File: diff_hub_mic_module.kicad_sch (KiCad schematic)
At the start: 4 parts, among them J6 RJ45, U11 MAX3485_SD

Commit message: Fixed most ERC checks
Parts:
- renumbered C13 to C12, J6 to J4, U11 to U6
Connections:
- no-connect marks 0 -> 1
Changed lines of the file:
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@@
 		(color 0 0 0 0)
+	)
+	(no_connect
+		(at 92.71 63.5)
 	)
 	(wire
@@
 		(dnp no)
 		(fields_autoplaced yes)
-		(property "Reference" "#PWR050"
+		(property "Reference" "#PWR041"
 			(at 90.17 46.99 0)
 			(effects
@@
 			(project "AEC_Speaker_Mic_System"
 				(path "/b4ee80b5-9d9a-4551-9b0c-6a8cb8d78ca3/ff66f788-06df-4fa5-89ad-7a9539b69b02/4ec81307-e110-499c-8742-d662ba3b7e0b"
-					(reference "#PWR060")
+					(reference "#PWR051")
 					(unit 1)
 				)
 				(path "/b4ee80b5-9d9a-4551-9b0c-6a8cb8d78ca3/ff66f788-06df-4fa5-89ad-7a9539b69b02/9b23b194-3f15-4ab8-af8d-e9f0a2683966"
-					(reference "#PWR065")
+					(reference "#PWR056")
 					(unit 1)
 				)
 				(path "/b4ee80b5-9d9a-4551-9b0c-6a8cb8d78ca3/ff66f788-06df-4fa5-89ad-7a9539b69b02/a06cf9bb-2ae0-4081-99cc-d8b6234c3557"
-					(reference "#PWR055")
+					(reference "#PWR046")
 					(unit 1)
 				)
 				(path "/b4ee80b5-9d9a-4551-9b0c-6a8cb8d78ca3/ff66f788-06df-4fa5-89ad-7a9539b69b02/e9f22984-330c-410d-9c8a-778be080e49d"
-					(reference "#PWR050")
+					(reference "#PWR041")
 					(unit 1)
 				)
@@
 		(dnp no)
 		(fields_autoplaced yes)
-		(property "Reference" "#PWR048"
+		(property "Reference" "#PWR039"
 			(at 67.31 50.8 0)
 			(effects
@@
 			(project "AEC_Speaker_Mic_System"
 				(path "/b4ee80b5-9d9a-4551-9b0c-6a8cb8d78ca3/ff66f788-06df-4fa5-89ad-7a9539b69b02/4ec81307-e110-499c-8742-d662ba3b7e0b"
-					(reference "#PWR058")
+					(reference "#PWR049")
 					(unit 1)
 				)
 				(path "/b4ee80b5-9d9a-4551-9b0c-6a8cb8d78ca3/ff66f788-06df-4fa5-89ad-7a9539b69b02/9b23b194-3f15-4ab8-af8d-e9f0a2683966"
-					(reference "#PWR063")
+					(reference "#PWR054")
 					(unit 1)
 				)
 				(path "/b4ee80b5-9d9a-4551-9b0c-6a8cb8d78ca3/ff66f788-06df-4fa5-89ad-7a9539b69b02/a06cf9bb-2ae0-4081-99cc-d8b6234c3557"
-					(reference "#PWR053")
+					(reference "#PWR044")
 					(unit 1)
 				)
 				(path "/b4ee80b5-9d9a-4551-9b0c-6a8cb8d78ca3/ff66f788-06df-4fa5-89ad-7a9539b69b02/e9f22984-330c-410d-9c8a-778be080e49d"
-					(reference "#PWR048")
+					(reference "#PWR039")
 					(unit 1)
 				)
@@
 		(dnp no)
 		(fields_autoplaced yes)
-		(property "Reference" "#PWR049"
+		(property "Reference" "#PWR040"
 			(at 77.47 53.34 0)
 			(effects
@@
 			(project "AEC_Speaker_Mic_System"
 				(path "/b4ee80b5-9d9a-4551-9b0c-6a8cb8d78ca3/ff66f788-06df-4fa5-89ad-7a9539b69b02/4ec81307-e110-499c-8742-d662ba3b7e0b"
-					(reference "#PWR059")
+					(reference "#PWR050")
 					(unit 1)
 				)
 				(path "/b4ee80b5-9d9a-4551-9b0c-6a8cb8d78ca3/ff66f788-06df-4fa5-89ad-7a9539b69b02/9b23b194-3f15-4ab8-af8d-e9f0a2683966"
-					(reference "#PWR064")
+					(reference "#PWR055")
 					(unit 1)
 				)
 				(path "/b4ee80b5-9d9a-4551-9b0c-6a8cb8d78ca3/ff66f788-06df-4fa5-89ad-7a9539b69b02/a06cf9bb-2ae0-4081-99cc-d8b6234c3557"
-					(reference "#PWR054")
+					(reference "#PWR045")
 					(unit 1)
 				)
 				(path "/b4ee80b5-9d9a-4551-9b0c-6a8cb8d78ca3/ff66f788-06df-4fa5-89ad-7a9539b69b02/e9f22984-330c-410d-9c8a-778be080e49d"
-					(reference "#PWR049")
+					(reference "#PWR040")
 					(unit 1)
 				)
@@
 		(dnp no)
 		(fields_autoplaced yes)
-		(property "Reference" "#PWR052"
+		(property "Reference" "#PWR043"
 			(at 102.87 80.01 0)
 			(effects
@@
 			(project "AEC_Speaker_Mic_System"
 				(path "/b4ee80b5-9d9a-4551-9b0c-6a8cb8d78ca3/ff66f788-06df-4fa5-89ad-7a9539b69b02/4ec81307-e110-499c-8742-d662ba3b7e0b"
-					(reference "#PWR062")
+					(reference "#PWR053")
 					(unit 1)
 				)
 				(path "/b4ee80b5-9d9a-4551-9b0c-6a8cb8d78ca3/ff66f788-06df-4fa5-89ad-7a9539b69b02/9b23b194-3f15-4ab8-af8d-e9f0a2683966"
-					(reference "#PWR067")
+					(reference "#PWR058")
 					(unit 1)
 				)
 				(path "/b4ee80b5-9d9a-4551-9b0c-6a8cb8d78ca3/ff66f788-06df-4fa5-89ad-7a9539b69b02/a06cf9bb-2ae0-4081-99cc-d8b6234c3557"
-					(reference "#PWR057")
+					(reference "#PWR048")
 					(unit 1)
 				)
 				(path "/b4ee80b5-9d9a-4551-9b0c-6a8cb8d78ca3/ff66f788-06df-4fa5-89ad-7a9539b69b02/e9f22984-330c-410d-9c8a-778be080e49d"
-					(reference "#PWR052")
+					(reference "#PWR043")
 					(unit 1)
 				)
@@
 		(dnp no)
 		(fields_autoplaced yes)
-		(property "Reference" "C13"
+		(property "Reference" "C12"
 			(at 100.33 38.0999 0)
 			(effects
@@
 			(project "AEC_Speaker_Mic_System"
 				(path "/b4ee80b5-9d9a-4551-9b0c-6a8cb8d78ca3/ff66f788-06df-4fa5-89ad-7a9539b69b02/4ec81307-e110-499c-8742-d662ba3b7e0b"
+					(reference "C14")
+					(unit 1)
+				)
+				(path "/b4ee80b5-9d9a-4551-9b0c-6a8cb8d78ca3/ff66f788-06df-4fa5-89ad-7a9539b69b02/9b23b194-3f15-4ab8-af8d-e9f0a2683966"
 					(reference "C15")
 					(unit 1)
 				)
-				(path "/b4ee80b5-9d9a-4551-9b0c-6a8cb8d78ca3/ff66f788-06df-4fa5-89ad-7a9539b69b02/9b23b194-3f15-4ab8-af8d-e9f0a2683966"
-					(reference "C16")
-					(unit 1)
-				)
 				(path "/b4ee80b5-9d9a-4551-9b0c-6a8cb8d78ca3/ff66f788-06df-4fa5-89ad-7a9539b69b02/a06cf9bb-2ae0-4081-99cc-d8b6234c3557"
-					(reference "C14")
+					(reference "C13")
 					(unit 1)
 				)
 				(path "/b4ee80b5-9d9a-4551-9b0c-6a8cb8d78ca3/ff66f788-06df-4fa5-89ad-7a9539b69b02/e9f22984-330c-410d-9c8a-778be080e49d"
-					(reference "C13")
+					(reference "C12")
 					(unit 1)
 				)
@@
 		(dnp no)
 		(fields_autoplaced yes)
-		(property "Reference" "#PWR051"
+		(property "Reference" "#PWR042"
 			(at 102.87 35.56 0)
 			(effects
@@
 			(project "AEC_Speaker_Mic_System"
 				(path "/b4ee80b5-9d9a-4551-9b0c-6a8cb8d78ca3/ff66f788-06df-4fa5-89ad-7a9539b69b02/4ec81307-e110-499c-8742-d662ba3b7e0b"
-					(reference "#PWR061")
+					(reference "#PWR052")
 					(unit 1)
 				)
 				(path "/b4ee80b5-9d9a-4551-9b0c-6a8cb8d78ca3/ff66f788-06df-4fa5-89ad-7a9539b69b02/9b23b194-3f15-4ab8-af8d-e9f0a2683966"
-					(reference "#PWR066")
+					(reference "#PWR057")
 					(unit 1)
 				)
 				(path "/b4ee80b5-9d9a-4551-9b0c-6a8cb8d78ca3/ff66f788-06df-4fa5-89ad-7a9539b69b02/a06cf9bb-2ae0-4081-99cc-d8b6234c3557"
-					(reference "#PWR056")
+					(reference "#PWR047")
 					(unit 1)
 				)
 				(path "/b4ee80b5-9d9a-4551-9b0c-6a8cb8d78ca3/ff66f788-06df-4fa5-89ad-7a9539b69b02/e9f22984-330c-410d-9c8a-778be080e49d"
-					(reference "#PWR051")
+					(reference "#PWR042")
 					(unit 1)
 				)
@@
 		(dnp no)
 		(fields_autoplaced yes)
-		(property "Reference" "J6"
+		(property "Reference" "J4"
 			(at 60.96 43.18 0)
 			(effects
@@
 			(project "AEC_Speaker_Mic_System"
 				(path "/b4ee80b5-9d9a-4551-9b0c-6a8cb8d78ca3/ff66f788-06df-4fa5-89ad-7a9539b69b02/4ec81307-e110-499c-8742-d662ba3b7e0b"
-					(reference "J8")
+					(reference "J6")
 					(unit 1)
 				)
 				(path "/b4ee80b5-9d9a-4551-9b0c-6a8cb8d78ca3/ff66f788-06df-4fa5-89ad-7a9539b69b02/9b23b194-3f15-4ab8-af8d-e9f0a2683966"
-					(reference "J9")
+					(reference "J7")
 					(unit 1)
 				)
 				(path "/b4ee80b5-9d9a-4551-9b0c-6a8cb8d78ca3/ff66f788-06df-4fa5-89ad-7a9539b69b02/a06cf9bb-2ae0-4081-99cc-d8b6234c3557"
-					(reference "J7")
+					(reference "J5")
 					(unit 1)
 				)
 				(path "/b4ee80b5-9d9a-4551-9b0c-6a8cb8d78ca3/ff66f788-06df-4fa5-89ad-7a9539b69b02/e9f22984-330c-410d-9c8a-778be080e49d"
-					(reference "J6")
+					(reference "J4")
 					(unit 1)
 				)
@@
 		(dnp no)
 		(fields_autoplaced yes)
-		(property "Reference" "U11"
+		(property "Reference" "U6"
 			(at 105.0133 40.64 0)
 			(effects
@@
 			(project "AEC_Speaker_Mic_System"
 				(path "/b4ee80b5-9d9a-4551-9b0c-6a8cb8d78ca3/ff66f788-06df-4fa5-89ad-7a9539b69b02/4ec81307-e110-499c-8742-d662ba3b7e0b"
-					(reference "U13")
+					(reference "U8")
 					(unit 1)
 				)
 				(path "/b4ee80b5-9d9a-4551-9b0c-6a8cb8d78ca3/ff66f788-06df-4fa5-89ad-7a9539b69b02/9b23b194-3f15-4ab8-af8d-e9f0a2683966"
-					(reference "U14")
+					(reference "U9")
 					(unit 1)
 				)
 				(path "/b4ee80b5-9d9a-4551-9b0c-6a8cb8d78ca3/ff66f788-06df-4fa5-89ad-7a9539b69b02/a06cf9bb-2ae0-4081-99cc-d8b6234c3557"
-					(reference "U12")
+					(reference "U7")
 					(unit 1)
 				)
 				(path "/b4ee80b5-9d9a-4551-9b0c-6a8cb8d78ca3/ff66f788-06df-4fa5-89ad-7a9539b69b02/e9f22984-330c-410d-9c8a-778be080e49d"
-					(reference "U11")
-					(unit 1)
-				)
+					(reference "U6")
+					(unit 1)
+				)

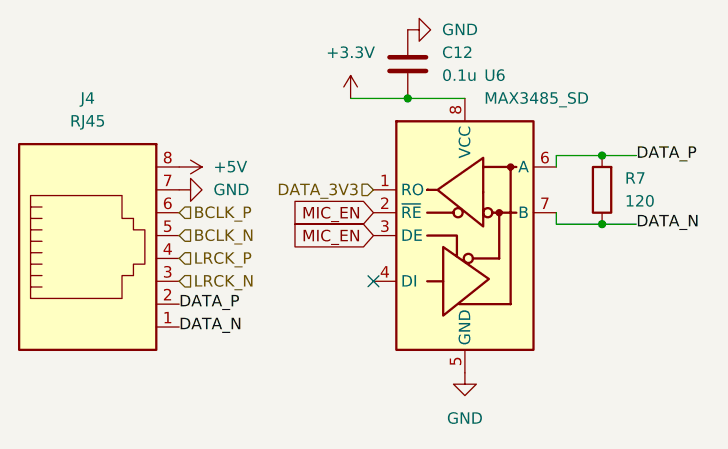
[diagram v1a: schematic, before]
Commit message: Footprinting done (warnings on schematic side but pcb import works fine)
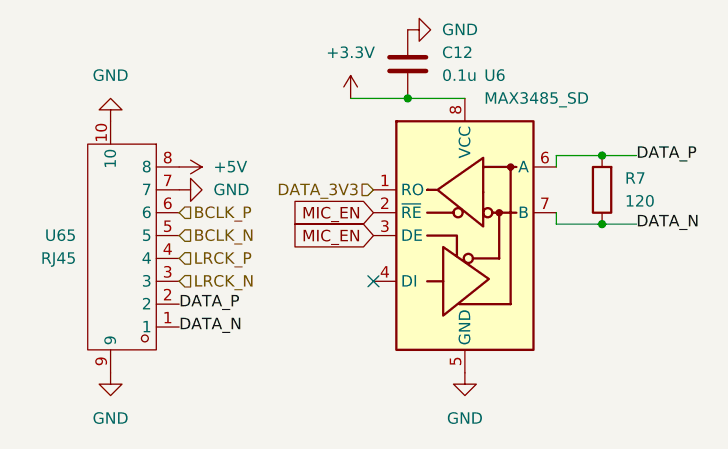
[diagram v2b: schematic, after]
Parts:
- removed J4: RJ45, symbol Connector:RJ45
- added U65: RJ45, Connector:RJ45-SMD_HC-RJ45-055-4_2, symbol Connector:HC-RJ45-055-4
- C12: footprint (none) -> Capacitor_SMD:C_0603_1608Metric
- R7: footprint (none) -> Resistor_SMD:R_0603_1608Metric
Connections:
- net +5V: now also U65.8
- net BCLK_N: now also U65.5
- net BCLK_P: now also U65.6
- net DATA_N: now also U65.1
- net DATA_P: now also U65.2
- net GND: now also U65.10, U65.7, U65.9
- net LRCK_N: now also U65.3
- net LRCK_P: now also U65.4
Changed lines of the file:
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@@
+	)
+	(symbol
+		(lib_id "Connector:HC-RJ45-055-4")
+		(at 66.04 58.42 180)
+		(unit 1)
+		(exclude_from_sim no)
+		(in_bom yes)
+		(on_board yes)
+		(dnp no)
+		(fields_autoplaced yes)
+		(property "Reference" "U65"
+			(at 59.69 58.4199 0)
+			(effects
+				(font
+					(size 1.27 1.27)
+				)
+				(justify left)
+			)
+		)
+		(property "Value" "RJ45"
+			(at 59.69 60.9599 0)
+			(effects
+				(font
+					(size 1.27 1.27)
+				)
+				(justify left)
+			)
+		)
+		(property "Footprint" "Connector:RJ45-SMD_HC-RJ45-055-4_2"
+			(at 66.04 58.42 0)
+			(effects
+				(font
+					(size 1.27 1.27)
+				)
+				(hide yes)
+			)
+		)
+		(property "Datasheet" "https://item.szlcsc.com/datasheet/HC-RJ45-055-4/3480994.html"
+			(at 66.04 58.42 0)
+			(effects
+				(font
+					(size 1.27 1.27)
+				)
+				(hide yes)
+			)
+		)
+		(property "Description" "Connector Type:RJ45 Jack Mounting Type:Recessed Mount Number of Ports:1 LED:Non-LED Shielding:Shielded Contact Material:Phosphor Bronze Contact Plating:Gold Operating Temperature:-40°C~+85°C Operating Temperature:-40°C~+85°C"
+			(at 66.04 58.42 0)
+			(effects
+				(font
+					(size 1.27 1.27)
+				)
+				(hide yes)
+			)
+		)
+		(property "Manufacturer Part" "HC-RJ45-055-4"
+			(at 66.04 58.42 0)
+			(effects
+				(font
+					(size 1.27 1.27)
+				)
+				(hide yes)
+			)
+		)
+		(property "Manufacturer" "HCTL(华灿天禄)"
+			(at 66.04 58.42 0)
+			(effects
+				(font
+					(size 1.27 1.27)
+				)
+				(hide yes)
+			)
+		)
+		(property "Supplier Part" "C3000211"
+			(at 66.04 58.42 0)
+			(effects
+				(font
+					(size 1.27 1.27)
+				)
+				(hide yes)
+			)
+		)
+		(property "Supplier" "LCSC"
+			(at 66.04 58.42 0)
+			(effects
+				(font
+					(size 1.27 1.27)
+				)
+				(hide yes)
+			)
+		)
+		(property "LCSC Part Name" "沉板 不带LED"
+			(at 66.04 58.42 0)
+			(effects
+				(font
+					(size 1.27 1.27)
+				)
+				(hide yes)
+			)
+		)
+		(pin "7"
+		)
+		(pin "5"
+		)
+		(pin "1"
+		)
+		(pin "3"
+		)
+		(pin "4"
+		)
+		(pin "10"
+		)
+		(pin "2"
+		)
+		(pin "8"
+		)
+		(pin "6"
+		)
+		(pin "9"
+		)
+		(instances
+			(project ""
+				(path "/b4ee80b5-9d9a-4551-9b0c-6a8cb8d78ca3/ff66f788-06df-4fa5-89ad-7a9539b69b02/4ec81307-e110-499c-8742-d662ba3b7e0b"
+					(reference "U67")
+					(unit 1)
+				)
+				(path "/b4ee80b5-9d9a-4551-9b0c-6a8cb8d78ca3/ff66f788-06df-4fa5-89ad-7a9539b69b02/9b23b194-3f15-4ab8-af8d-e9f0a2683966"
+					(reference "U68")
+					(unit 1)
+				)
+				(path "/b4ee80b5-9d9a-4551-9b0c-6a8cb8d78ca3/ff66f788-06df-4fa5-89ad-7a9539b69b02/a06cf9bb-2ae0-4081-99cc-d8b6234c3557"
+					(reference "U66")
+					(unit 1)
+				)
+				(path "/b4ee80b5-9d9a-4551-9b0c-6a8cb8d78ca3/ff66f788-06df-4fa5-89ad-7a9539b69b02/e9f22984-330c-410d-9c8a-778be080e49d"
+					(reference "U65")
+					(unit 1)
+				)
+			)
+		)
 	)
 	(symbol
@@
 	)
 	(symbol
+		(lib_id "power:GND")
+		(at 63.5 45.72 180)
+		(unit 1)
+		(exclude_from_sim no)
+		(in_bom yes)
+		(on_board yes)
+		(dnp no)
+		(fields_autoplaced yes)
+		(property "Reference" "#PWR0465"
+			(at 63.5 39.37 0)
+			(effects
+				(font
+					(size 1.27 1.27)
+				)
+				(hide yes)
+			)
+		)
+		(property "Value" "GND"
+			(at 63.5 40.64 0)
+			(effects
+				(font
+					(size 1.27 1.27)
+				)
+			)
+		)
+		(property "Footprint" ""
+			(at 63.5 45.72 0)
+			(effects
+				(font
+					(size 1.27 1.27)
+				)
+				(hide yes)
+			)
+		)
+		(property "Datasheet" ""
+			(at 63.5 45.72 0)
+			(effects
+				(font
+					(size 1.27 1.27)
+				)
+				(hide yes)
+			)
+		)
+		(property "Description" "Power symbol creates a global label with name \"GND\" , ground"
+			(at 63.5 45.72 0)
+			(effects
+				(font
+					(size 1.27 1.27)
+				)
+				(hide yes)
+			)
+		)
+		(pin "1"
+		)
+		(instances
+			(project ""
+				(path "/b4ee80b5-9d9a-4551-9b0c-6a8cb8d78ca3/ff66f788-06df-4fa5-89ad-7a9539b69b02/4ec81307-e110-499c-8742-d662ba3b7e0b"
+					(reference "#PWR0467")
+					(unit 1)
+				)
+				(path "/b4ee80b5-9d9a-4551-9b0c-6a8cb8d78ca3/ff66f788-06df-4fa5-89ad-7a9539b69b02/9b23b194-3f15-4ab8-af8d-e9f0a2683966"
+					(reference "#PWR0468")
+					(unit 1)
+				)
+				(path "/b4ee80b5-9d9a-4551-9b0c-6a8cb8d78ca3/ff66f788-06df-4fa5-89ad-7a9539b69b02/a06cf9bb-2ae0-4081-99cc-d8b6234c3557"
+					(reference "#PWR0466")
+					(unit 1)
+				)
+				(path "/b4ee80b5-9d9a-4551-9b0c-6a8cb8d78ca3/ff66f788-06df-4fa5-89ad-7a9539b69b02/e9f22984-330c-410d-9c8a-778be080e49d"
+					(reference "#PWR0465")
+					(unit 1)
+				)
+			)
+		)
+	)
+	(symbol
 		(lib_id "Device:R")
 		(at 118.11 53.34 180)
@@
 			)
 		)
-		(property "Footprint" ""
+		(property "Footprint" "Resistor_SMD:R_0603_1608Metric"
 			(at 119.888 53.34 90)
 			(effects
@@
 			)
 		)
-		(property "Footprint" ""
+		(property "Footprint" "Capacitor_SMD:C_0603_1608Metric"
 			(at 97.4852 43.18 0)
 			(effects
@@
 	)
 	(symbol
-		(lib_id "Connector:RJ45")
-		(at 60.96 60.96 0)
-		(unit 1)
-		(exclude_from_sim no)
-		(in_bom yes)
-		(on_board yes)
-		(dnp no)
-		(fields_autoplaced yes)
-		(property "Reference" "J4"
-			(at 60.96 43.18 0)
-			(effects
-				(font
-					(size 1.27 1.27)
-				)
-			)
-		)
-		(property "Value" "RJ45"
-			(at 60.96 45.72 0)
+		(lib_id "power:GND")
+		(at 63.5 73.66 0)
+		(unit 1)
+		(exclude_from_sim no)
+		(in_bom yes)
+		(on_board yes)
+		(dnp no)
+		(fields_autoplaced yes)
+		(property "Reference" "#PWR0461"
+			(at 63.5 80.01 0)
+			(effects
+				(font
+					(size 1.27 1.27)
+				)
+				(hide yes)
+			)
+		)
+		(property "Value" "GND"
+			(at 63.5 78.74 0)
 			(effects
 				(font
@@
 		)
 		(property "Footprint" ""
-			(at 60.96 60.325 90)
-			(effects
-				(font
-					(size 1.27 1.27)
-				)
-				(hide yes)
-			)
-		)
-		(property "Datasheet" "~"
-			(at 60.96 60.325 90)
-			(effects
-				(font
-					(size 1.27 1.27)
-				)
-				(hide yes)
-			)
-		)
-		(property "Description" "RJ connector, 8P8C (8 positions 8 connected)"
-			(at 60.96 60.96 0)
-			(effects
-				(font
-					(size 1.27 1.27)
-				)
-				(hide yes)
-			)
-		)
-		(pin "2"
-		)
-		(pin "6"
-		)
-		(pin "4"
-		)
-		(pin "3"
-		)
-		(pin "8"
-		)
-		(pin "7"
-		)
-		(pin "1"
-		)
-		(pin "5"
-		)
-		(instances
-			(project "AEC_Speaker_Mic_System"
-				(path "/b4ee80b5-9d9a-4551-9b0c-6a8cb8d78ca3/ff66f788-06df-4fa5-89ad-7a9539b69b02/4ec81307-e110-499c-8742-d662ba3b7e0b"
-					(reference "J6")
-					(unit 1)
-				)
-				(path "/b4ee80b5-9d9a-4551-9b0c-6a8cb8d78ca3/ff66f788-06df-4fa5-89ad-7a9539b69b02/9b23b194-3f15-4ab8-af8d-e9f0a2683966"
-					(reference "J7")
-					(unit 1)
-				)
-				(path "/b4ee80b5-9d9a-4551-9b0c-6a8cb8d78ca3/ff66f788-06df-4fa5-89ad-7a9539b69b02/a06cf9bb-2ae0-4081-99cc-d8b6234c3557"
-					(reference "J5")
-					(unit 1)
-				)
-				(path "/b4ee80b5-9d9a-4551-9b0c-6a8cb8d78ca3/ff66f788-06df-4fa5-89ad-7a9539b69b02/e9f22984-330c-410d-9c8a-778be080e49d"
-					(reference "J4")
-					(unit 1)
-				)
+			(at 63.5 73.66 0)
+			(effects
+				(font
+					(size 1.27 1.27)
+				)
+				(hide yes)
+			)
+		)
+		(property "Datasheet" ""
+			(at 63.5 73.66 0)
+			(effects
+				(font
+					(size 1.27 1.27)
+				)
+				(hide yes)
+			)
+		)
+		(property "Description" "Power symbol creates a global label with name \"GND\" , ground"
+			(at 63.5 73.66 0)
+			(effects
+				(font
+					(size 1.27 1.27)
+				)
+				(hide yes)
+			)
+		)
+		(pin "1"
+		)
+		(instances
+			(project ""
+				(path "/b4ee80b5-9d9a-4551-9b0c-6a8cb8d78ca3/ff66f788-06df-4fa5-89ad-7a9539b69b02/4ec81307-e110-499c-8742-d662ba3b7e0b"
+					(reference "#PWR0463")
+					(unit 1)
+				)
+				(path "/b4ee80b5-9d9a-4551-9b0c-6a8cb8d78ca3/ff66f788-06df-4fa5-89ad-7a9539b69b02/9b23b194-3f15-4ab8-af8d-e9f0a2683966"
+					(reference "#PWR0464")
+					(unit 1)
+				)
+				(path "/b4ee80b5-9d9a-4551-9b0c-6a8cb8d78ca3/ff66f788-06df-4fa5-89ad-7a9539b69b02/a06cf9bb-2ae0-4081-99cc-d8b6234c3557"
+					(reference "#PWR0462")
+					(unit 1)
+				)
+				(path "/b4ee80b5-9d9a-4551-9b0c-6a8cb8d78ca3/ff66f788-06df-4fa5-89ad-7a9539b69b02/e9f22984-330c-410d-9c8a-778be080e49d"
+					(reference "#PWR0461")
+					(unit 1)
+				)

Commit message: Minor schematic changes
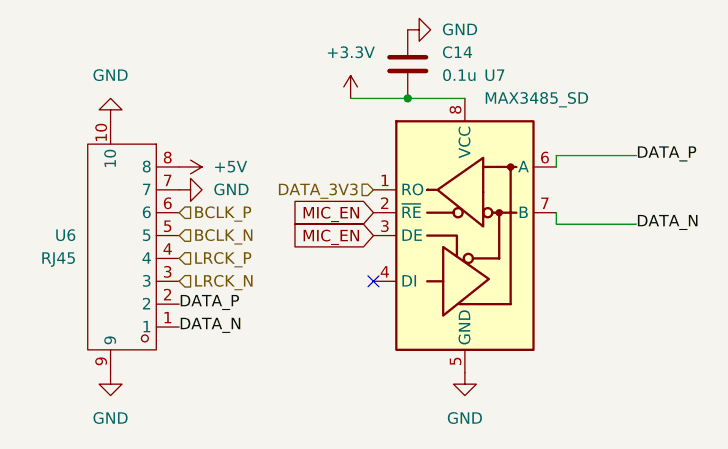
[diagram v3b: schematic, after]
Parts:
- removed R7: 120, Resistor_SMD:R_0603_1608Metric, symbol Device:R
- renumbered C12 to C14, U65 to U6, U6 to U7
